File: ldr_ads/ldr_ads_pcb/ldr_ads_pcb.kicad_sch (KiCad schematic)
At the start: 5 parts, among them J1 Conn_01x03

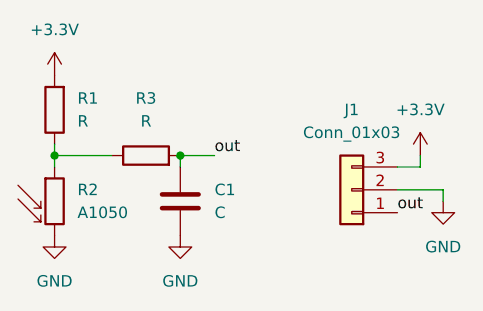
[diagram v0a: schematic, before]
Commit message: changed ldr pcb
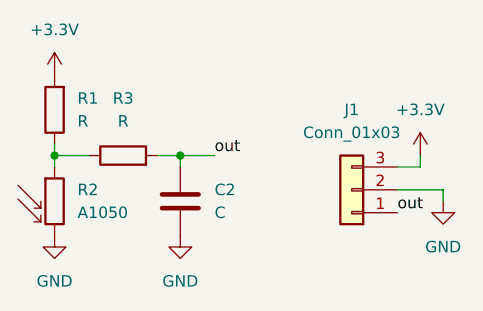
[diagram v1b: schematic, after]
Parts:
- removed C1: C, Capacitor_THT:C_Rect_L4.6mm_W2.0mm_P2.50mm_MKS02_FKP02, symbol Device:C
- added C2: C, Capacitor_THT:C_Rect_L7.2mm_W3.5mm_P5.00mm_FKS2_FKP2_MKS2_MKP2, symbol Device:C
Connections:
- net GND: now also C2.2
- net out: now also C2.1
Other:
- moved on the sheet: R3
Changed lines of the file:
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@@
+	(wire
+		(pts
+			(xy 62.23 52.07) (xy 64.77 52.07)
+		)
+		(stroke
+			(width 0)
+			(type default)
+		)
+	)
 	(wire
 		(pts
@@
 	(wire
 		(pts
-			(xy 57.15 52.07) (xy 50.8 52.07)
+			(xy 54.61 52.07) (xy 50.8 52.07)
 		)
 		(stroke
@@
 		(dnp no)
 		(fields_autoplaced yes)
-		(property "Reference" "C1"
+		(property "Reference" "C2"
 			(at 68.58 55.8799 0)
 			(effects
@@
 			)
 		)
-		(property "Footprint" "Capacitor_THT:C_Rect_L4.6mm_W2.0mm_P2.50mm_MKS02_FKP02"
+		(property "Footprint" "Capacitor_THT:C_Rect_L7.2mm_W3.5mm_P5.00mm_FKS2_FKP2_MKS2_MKP2"
 			(at 65.7352 60.96 0)
 			(effects
@@
 			(project ""
 				(path "/4c4828b4-32ca-4ff2-8f5a-f2a5abe04123"
-					(reference "C1")
+					(reference "C2")
 					(unit 1)
 				)
@@
 	(symbol
 		(lib_id "Device:R")
-		(at 60.96 52.07 90)
+		(at 58.42 52.07 90)
 		(unit 1)
 		(exclude_from_sim no)
@@
 		(fields_autoplaced yes)
 		(property "Reference" "R3"
-			(at 60.96 45.72 90)
+			(at 58.42 45.72 90)
 			(effects
 				(font
@@
 		)
 		(property "Value" "R"
-			(at 60.96 48.26 90)
+			(at 58.42 48.26 90)
 			(effects
 				(font
@@
 		)
 		(property "Footprint" "Resistor_THT:R_Axial_DIN0414_L11.9mm_D4.5mm_P15.24mm_Horizontal"
-			(at 60.96 53.848 90)
+			(at 58.42 53.848 90)
 			(effects
 				(font
@@
 		)
 		(property "Datasheet" "~"
-			(at 60.96 52.07 0)
+			(at 58.42 52.07 0)
 			(effects
 				(font
@@
 		)
 		(property "Description" "Resistor"
-			(at 60.96 52.07 0)
-			(effects
-				(font
+			(at 58.42 52.07 0)
+			(effects
+				(font

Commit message: changed schematic
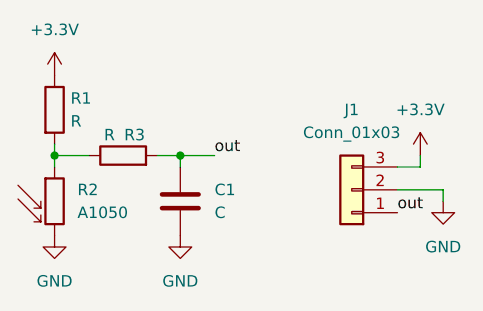
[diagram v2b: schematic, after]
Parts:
- R1, R3: footprint Resistor_THT:R_Axial_DIN0414_L11.9mm_D4.5mm_P15.24mm_Horizontal -> Resistor_THT:R_Axial_DIN0207_L6.3mm_D2.5mm_P10.16mm_Horizontal
- renumbered C2 to C1
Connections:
- net +3.3V: now also R1.1; no longer R1.2
- net at R2.1, R3.1: now also R1.2; no longer R1.1
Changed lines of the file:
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@@
-	)
-	(symbol
-		(lib_id "Device:R")
-		(at 50.8 46.99 180)
-		(unit 1)
-		(exclude_from_sim no)
-		(in_bom yes)
-		(on_board yes)
-		(dnp no)
-		(fields_autoplaced yes)
-		(property "Reference" "R1"
-			(at 53.34 45.7199 0)
-			(effects
-				(font
-					(size 1.27 1.27)
-				)
-				(justify right)
-			)
-		)
-		(property "Value" "R"
-			(at 53.34 48.2599 0)
-			(effects
-				(font
-					(size 1.27 1.27)
-				)
-				(justify right)
-			)
-		)
-		(property "Footprint" "Resistor_THT:R_Axial_DIN0414_L11.9mm_D4.5mm_P15.24mm_Horizontal"
-			(at 52.578 46.99 90)
-			(effects
-				(font
-					(size 1.27 1.27)
-				)
-				(hide yes)
-			)
-		)
-		(property "Datasheet" "~"
-			(at 50.8 46.99 0)
-			(effects
-				(font
-					(size 1.27 1.27)
-				)
-				(hide yes)
-			)
-		)
-		(property "Description" "Resistor"
-			(at 50.8 46.99 0)
-			(effects
-				(font
-					(size 1.27 1.27)
-				)
-				(hide yes)
-			)
-		)
-		(pin "2"
-		)
-		(pin "1"
-		)
-		(instances
-			(project ""
-				(path "/4c4828b4-32ca-4ff2-8f5a-f2a5abe04123"
-					(reference "R1")
-					(unit 1)
-				)
-			)
-		)
 	)
 	(symbol
@@
 		(dnp no)
 		(fields_autoplaced yes)
-		(property "Reference" "C2"
+		(property "Reference" "C1"
 			(at 68.58 55.8799 0)
 			(effects
@@
 			(project ""
 				(path "/4c4828b4-32ca-4ff2-8f5a-f2a5abe04123"
-					(reference "C2")
+					(reference "C1")
+					(unit 1)
+				)
+			)
+		)
+	)
+	(symbol
+		(lib_id "Device:R")
+		(at 58.42 52.07 90)
+		(unit 1)
+		(exclude_from_sim no)
+		(in_bom yes)
+		(on_board yes)
+		(dnp no)
+		(property "Reference" "R3"
+			(at 59.69 49.784 90)
+			(effects
+				(font
+					(size 1.27 1.27)
+				)
+			)
+		)
+		(property "Value" "R"
+			(at 56.896 49.784 90)
+			(effects
+				(font
+					(size 1.27 1.27)
+				)
+			)
+		)
+		(property "Footprint" "Resistor_THT:R_Axial_DIN0207_L6.3mm_D2.5mm_P10.16mm_Horizontal"
+			(at 58.42 53.848 90)
+			(effects
+				(font
+					(size 1.27 1.27)
+				)
+				(hide yes)
+			)
+		)
+		(property "Datasheet" "~"
+			(at 58.42 52.07 0)
+			(effects
+				(font
+					(size 1.27 1.27)
+				)
+				(hide yes)
+			)
+		)
+		(property "Description" "Resistor"
+			(at 58.42 52.07 0)
+			(effects
+				(font
+					(size 1.27 1.27)
+				)
+				(hide yes)
+			)
+		)
+		(pin "1"
+		)
+		(pin "2"
+		)
+		(instances
+			(project ""
+				(path "/4c4828b4-32ca-4ff2-8f5a-f2a5abe04123"
+					(reference "R3")
 					(unit 1)
 				)
@@
 	)
 	(symbol
+		(lib_id "Device:R")
+		(at 50.8 46.99 0)
+		(unit 1)
+		(exclude_from_sim no)
+		(in_bom yes)
+		(on_board yes)
+		(dnp no)
+		(property "Reference" "R1"
+			(at 52.578 45.72 0)
+			(effects
+				(font
+					(size 1.27 1.27)
+				)
+				(justify left)
+			)
+		)
+		(property "Value" "R"
+			(at 52.578 48.26 0)
+			(effects
+				(font
+					(size 1.27 1.27)
+				)
+				(justify left)
+			)
+		)
+		(property "Footprint" "Resistor_THT:R_Axial_DIN0207_L6.3mm_D2.5mm_P10.16mm_Horizontal"
+			(at 49.022 46.99 90)
+			(effects
+				(font
+					(size 1.27 1.27)
+				)
+				(hide yes)
+			)
+		)
+		(property "Datasheet" "~"
+			(at 50.8 46.99 0)
+			(effects
+				(font
+					(size 1.27 1.27)
+				)
+				(hide yes)
+			)
+		)
+		(property "Description" "Resistor"
+			(at 50.8 46.99 0)
+			(effects
+				(font
+					(size 1.27 1.27)
+				)
+				(hide yes)
+			)
+		)
+		(pin "1"
+		)
+		(pin "2"
+		)
+		(instances
+			(project "ldr_ads_pcb"
+				(path "/4c4828b4-32ca-4ff2-8f5a-f2a5abe04123"
+					(reference "R1")
+					(unit 1)
+				)
+			)
+		)
+	)
+	(symbol
 		(lib_id "Connector_Generic:Conn_01x03")
 		(at 83.82 55.88 180)
@@
 					(unit 1)
 				)
-			)
-		)
-	)
-	(symbol
-		(lib_id "Device:R")
-		(at 58.42 52.07 90)
-		(unit 1)
-		(exclude_from_sim no)
-		(in_bom yes)
-		(on_board yes)
-		(dnp no)
-		(fields_autoplaced yes)
-		(property "Reference" "R3"
-			(at 58.42 45.72 90)
-			(effects
-				(font
-					(size 1.27 1.27)
-				)
-			)
-		)
-		(property "Value" "R"
-			(at 58.42 48.26 90)
-			(effects
-				(font
-					(size 1.27 1.27)
-				)
-			)
-		)
-		(property "Footprint" "Resistor_THT:R_Axial_DIN0414_L11.9mm_D4.5mm_P15.24mm_Horizontal"
-			(at 58.42 53.848 90)
-			(effects
-				(font
-					(size 1.27 1.27)
-				)
-				(hide yes)
-			)
-		)
-		(property "Datasheet" "~"
-			(at 58.42 52.07 0)
-			(effects
-				(font
-					(size 1.27 1.27)
-				)
-				(hide yes)
-			)
-		)
-		(property "Description" "Resistor"
-			(at 58.42 52.07 0)
-			(effects
-				(font
-					(size 1.27 1.27)
-				)
-				(hide yes)
-			)
-		)
-		(pin "1"
-		)
-		(pin "2"
-		)
-		(instances
-			(project ""
-				(path "/4c4828b4-32ca-4ff2-8f5a-f2a5abe04123"
-					(reference "R3")
-					(unit 1)
-				)
